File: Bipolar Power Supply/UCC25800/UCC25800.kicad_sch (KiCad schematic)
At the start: 0 parts

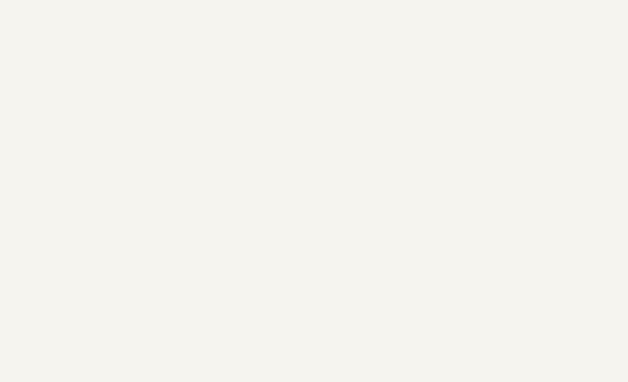
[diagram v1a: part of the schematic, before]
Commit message: UCC25800 : PCB layout
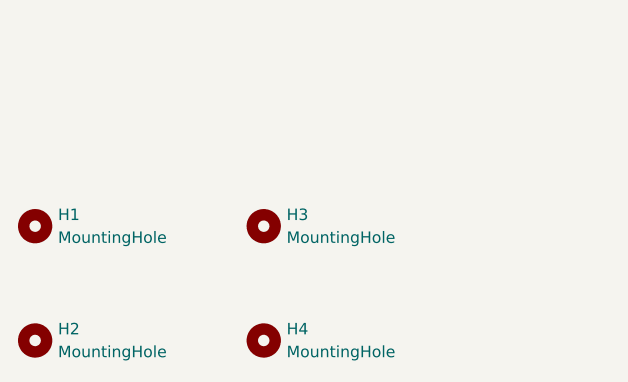
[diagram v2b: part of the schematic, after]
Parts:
- added H1, H2, H3, H4: MountingHole, MountingHole:MountingHole_2.5mm, symbol Mechanical:MountingHole
